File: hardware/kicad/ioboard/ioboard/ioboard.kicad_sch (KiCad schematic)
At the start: 0 parts

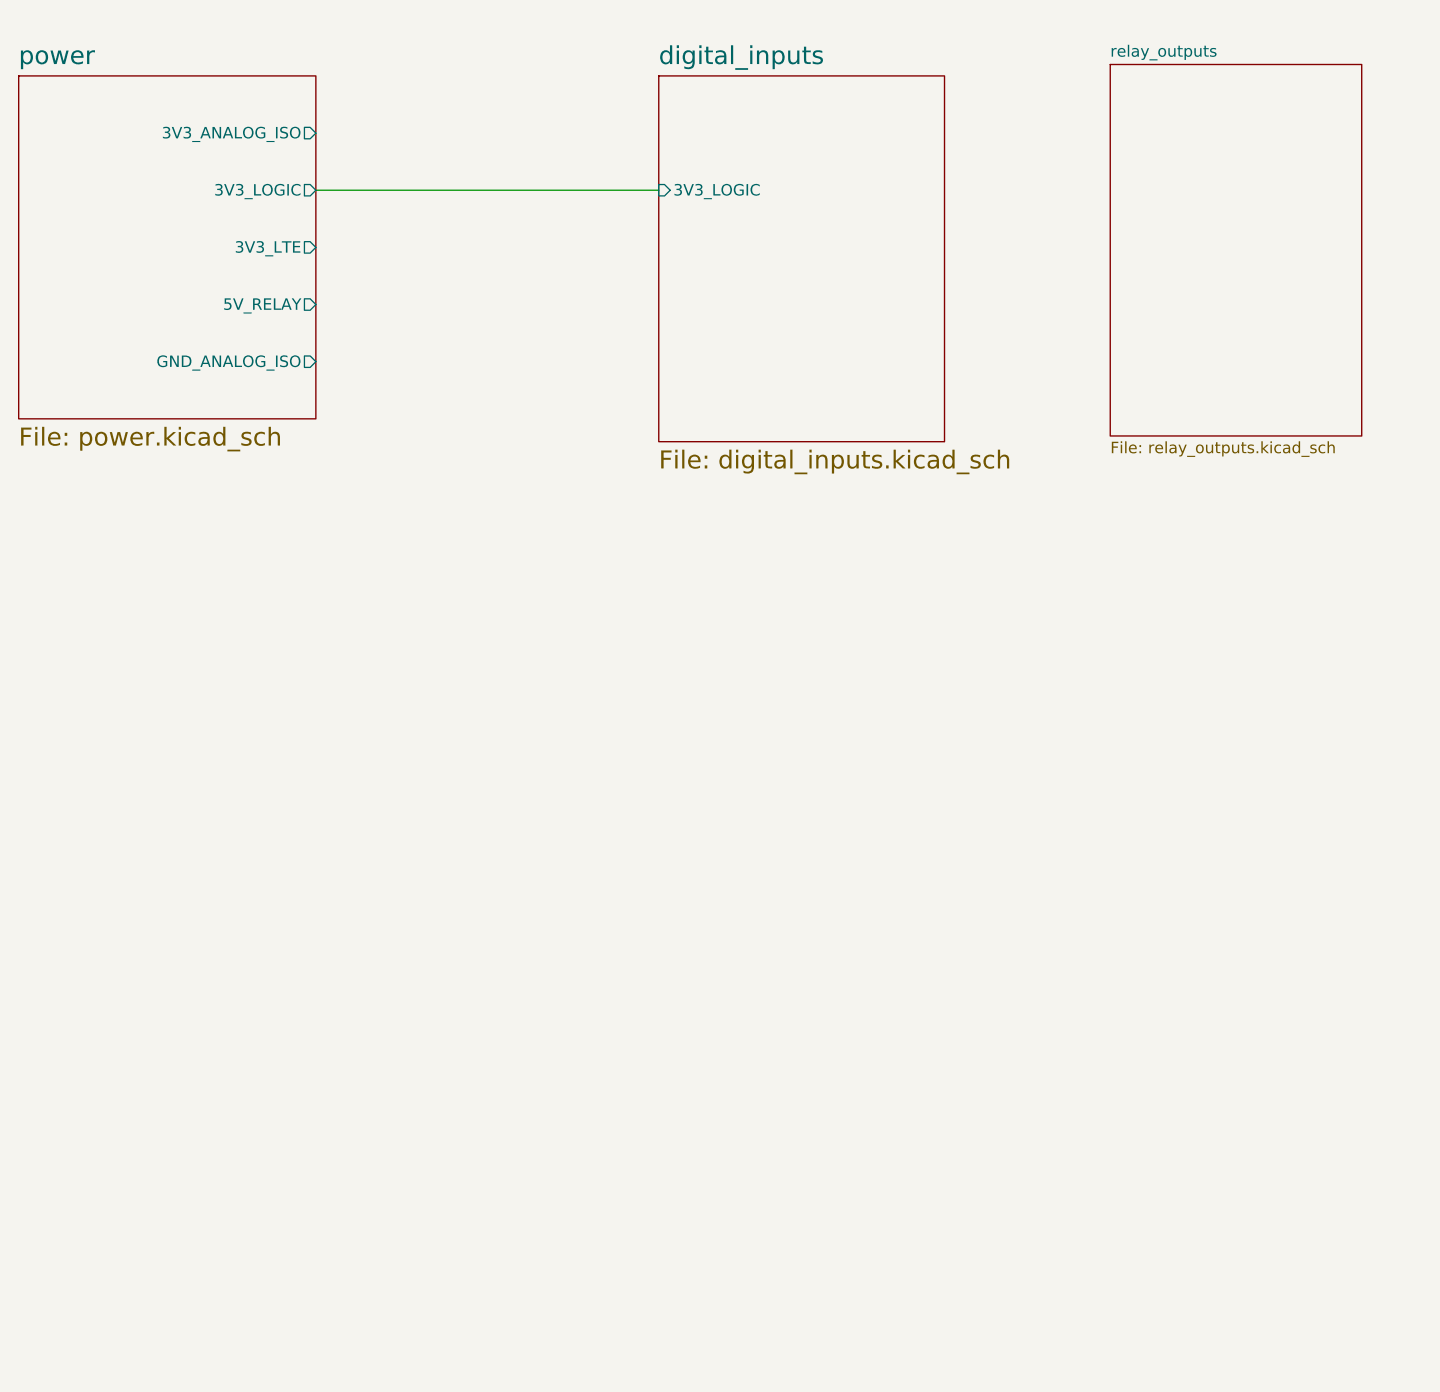
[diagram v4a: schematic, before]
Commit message: relay-outputs: schematic capture complete, plan closed out
All 4 channels wired: K1-K4 (Panasonic ALDP105) driven by Q1-Q4 (Nexperia
MMBT3904) through R26-R33 (510ohm base / 10k pull-down pairs) and D9-D12
(1N4148 flyback), contacts broken out independently to J3 (Phoenix Contact
MC 1,5/8-ST-3,5, 8 positions). Added C21/C22 (10uF/100nF bulk+bypass) at
the 5V_RELAY entry point for EMI/noise reasons -- documented as design
decision 5, with corrected reasoning (coil inductance already rate-limits
the current step, so this isn't about regulator transient response the
way core-compute's WiFi-burst caps were).

Root sheet now wires relay_outputs' 5V_RELAY hierarchical pin to power's
output, verified programmatically that the wire path actually joins both
pin coordinates. Caught and fixed a reversed flyback diode (D9) before
commit -- would have put a forward-biased diode across the coil the whole
time each transistor was on.

Also commits the imported ALDP105 KiCad symbol/footprint library (no
numbered pinout exists in any datasheet, so pin functions were verified
live against the placed symbol, same resolution used for the LTV-247).
The imported footprint has the right pad count but has NOT been
independently checked against the real part's mechanical drawing --
flagged explicitly in the plan doc and CLAUDE.md rather than assumed
correct just because it came from a library.

Documentation: relay-outputs.md completed through sign-off (schematic
capture, verification checklist, acceptance criteria, BOM, commissioning
items), new relay_outputs_bom.csv (23 parts, CSV-parse verified), and
hardware/kicad/README.md updated. ERC and footprint assignment (including
the ALDP105 footprint check) deferred to the same pre-merge pass as
digital-inputs, per the user's standing policy -- tracked in CLAUDE.md.

Co-Authored-By: Claude Sonnet 5 <noreply@anthropic.com>
Claude-Session: https://claude.ai/code/session_011Mk4ACKLUzGL8p2SUjrweQ
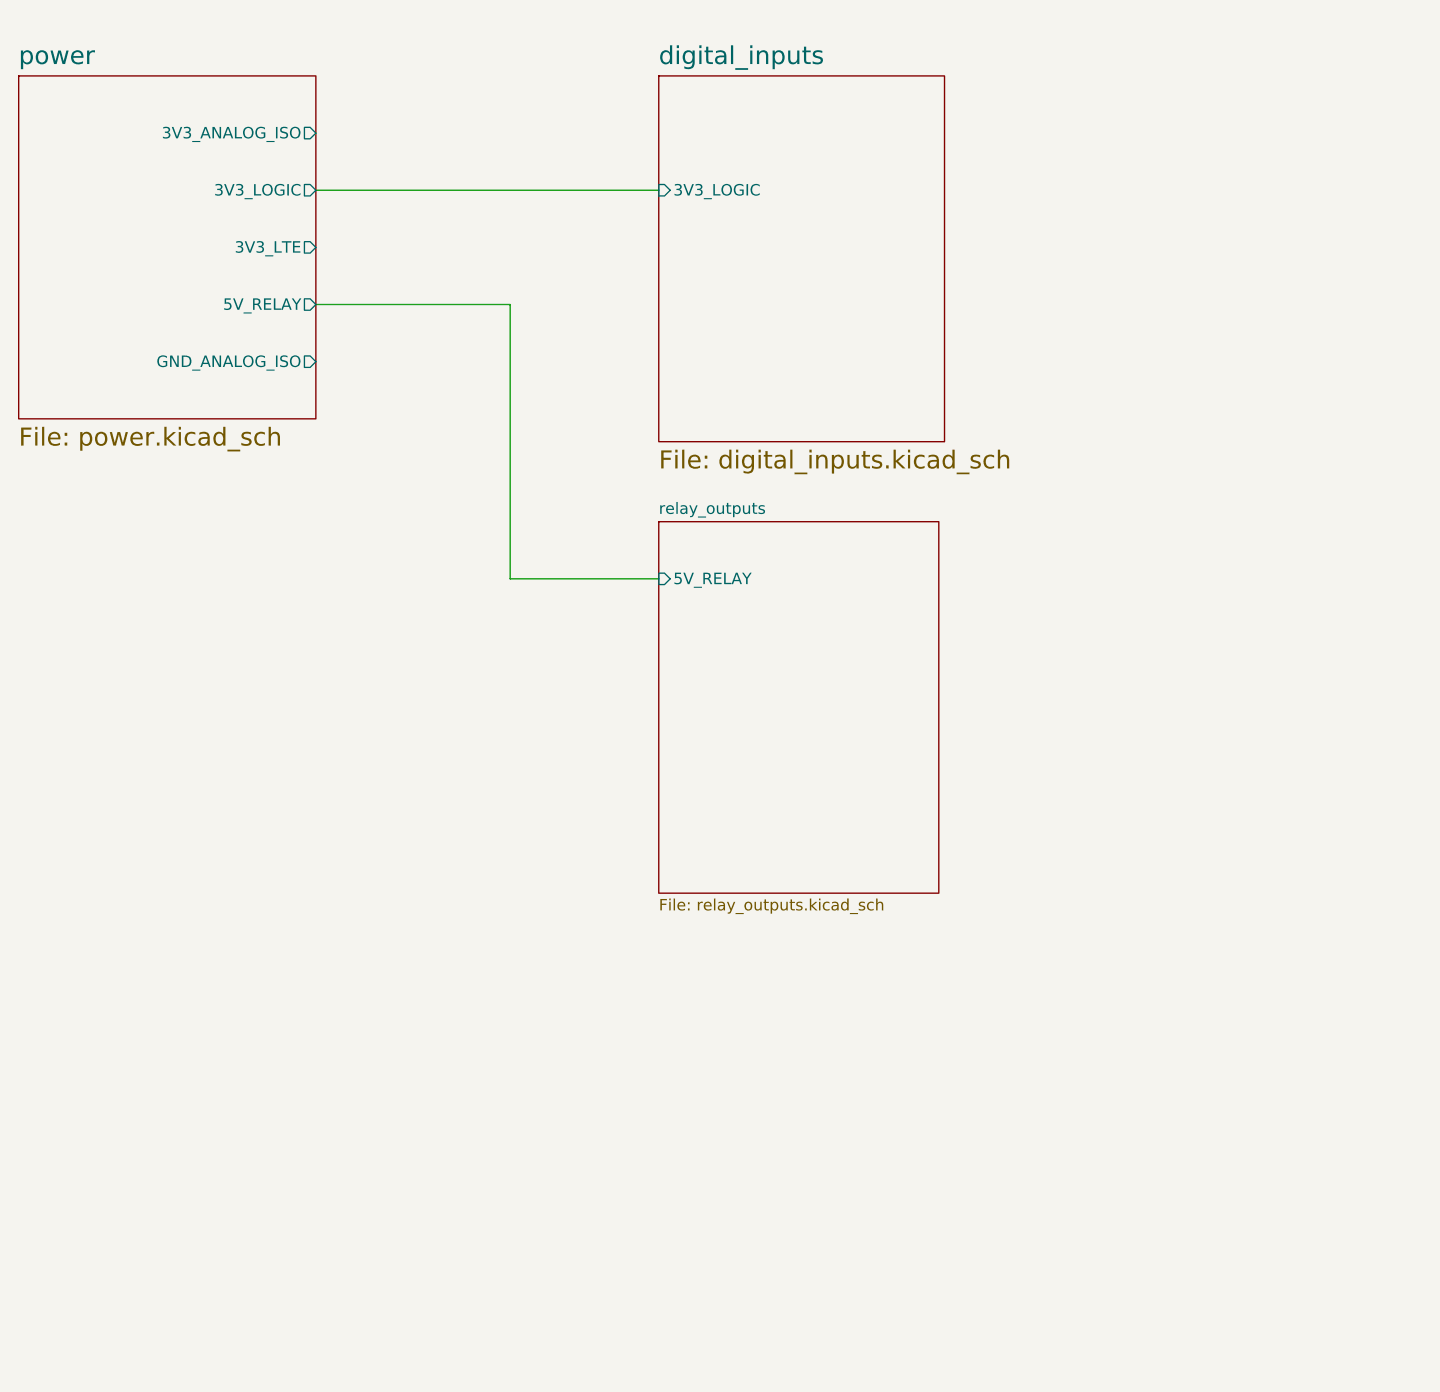
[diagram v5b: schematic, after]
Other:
- sheet relay_outputs ports: added 5V_RELAY; removed none
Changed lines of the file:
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@@
+	(wire
+		(pts
+			(xy 102.87 88.9) (xy 86.36 88.9)
+		)
+		(stroke
+			(width 0)
+			(type default)
+		)
+	)
 	(wire
 		(pts
@@
 		)
 	)
+	(wire
+		(pts
+			(xy 86.36 58.42) (xy 86.36 88.9)
+		)
+		(stroke
+			(width 0)
+			(type default)
+		)
+	)
+	(wire
+		(pts
+			(xy 64.77 58.42) (xy 86.36 58.42)
+		)
+		(stroke
+			(width 0)
+			(type default)
+		)
+	)
 	(sheet
-		(at 153.035 31.75)
-		(size 27.94 41.275)
+		(at 102.87 82.55)
+		(size 31.115 41.275)
 		(exclude_from_sim no)
 		(in_bom yes)
@@
 		)
 		(property "Sheetname" "relay_outputs"
-			(at 153.035 31.0384 0)
+			(at 102.87 81.8384 0)
 			(effects
 				(font
@@
 		)
 		(property "Sheetfile" "relay_outputs.kicad_sch"
-			(at 153.035 73.6096 0)
+			(at 102.87 124.4096 0)
 			(effects
 				(font
@@
 			)
 		)
+		(pin "5V_RELAY" input
+			(at 102.87 88.9 180)
+			(effects
+				(font
+					(size 1.27 1.27)
+				)
+				(justify left)
+			)
+		)

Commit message: analog-io: schematic capture complete, Step 6 verification started
Step 5: analog_io.kicad_sch built and verified pin-by-pin - ADS1115 ADC,
ISO1540 I2C isolator, MCP4725 DAC, 2x LM2904 physical packages (input
buffers + output gain stage), SMBJ15CA TVS protection per channel,
stuffing-option dividers, output feedback network, and the J4 field
connector. Root-sheet integration confirmed on ioboard.kicad_sch.

Two real issues caught and fixed during capture: an output-stage feedback
network wired to break the loop (R_f tied to GND instead of the -/R_in
node), and ambiguous resistor reference designators across the two input
channels.

Step 6: schematic-level verification checks done (address collisions,
ground-domain isolation, feedback topology); ERC and physical bring-up
checks still open.

Co-Authored-By: Claude Sonnet 5 <noreply@anthropic.com>
Claude-Session: https://claude.ai/code/session_011Mk4ACKLUzGL8p2SUjrweQ
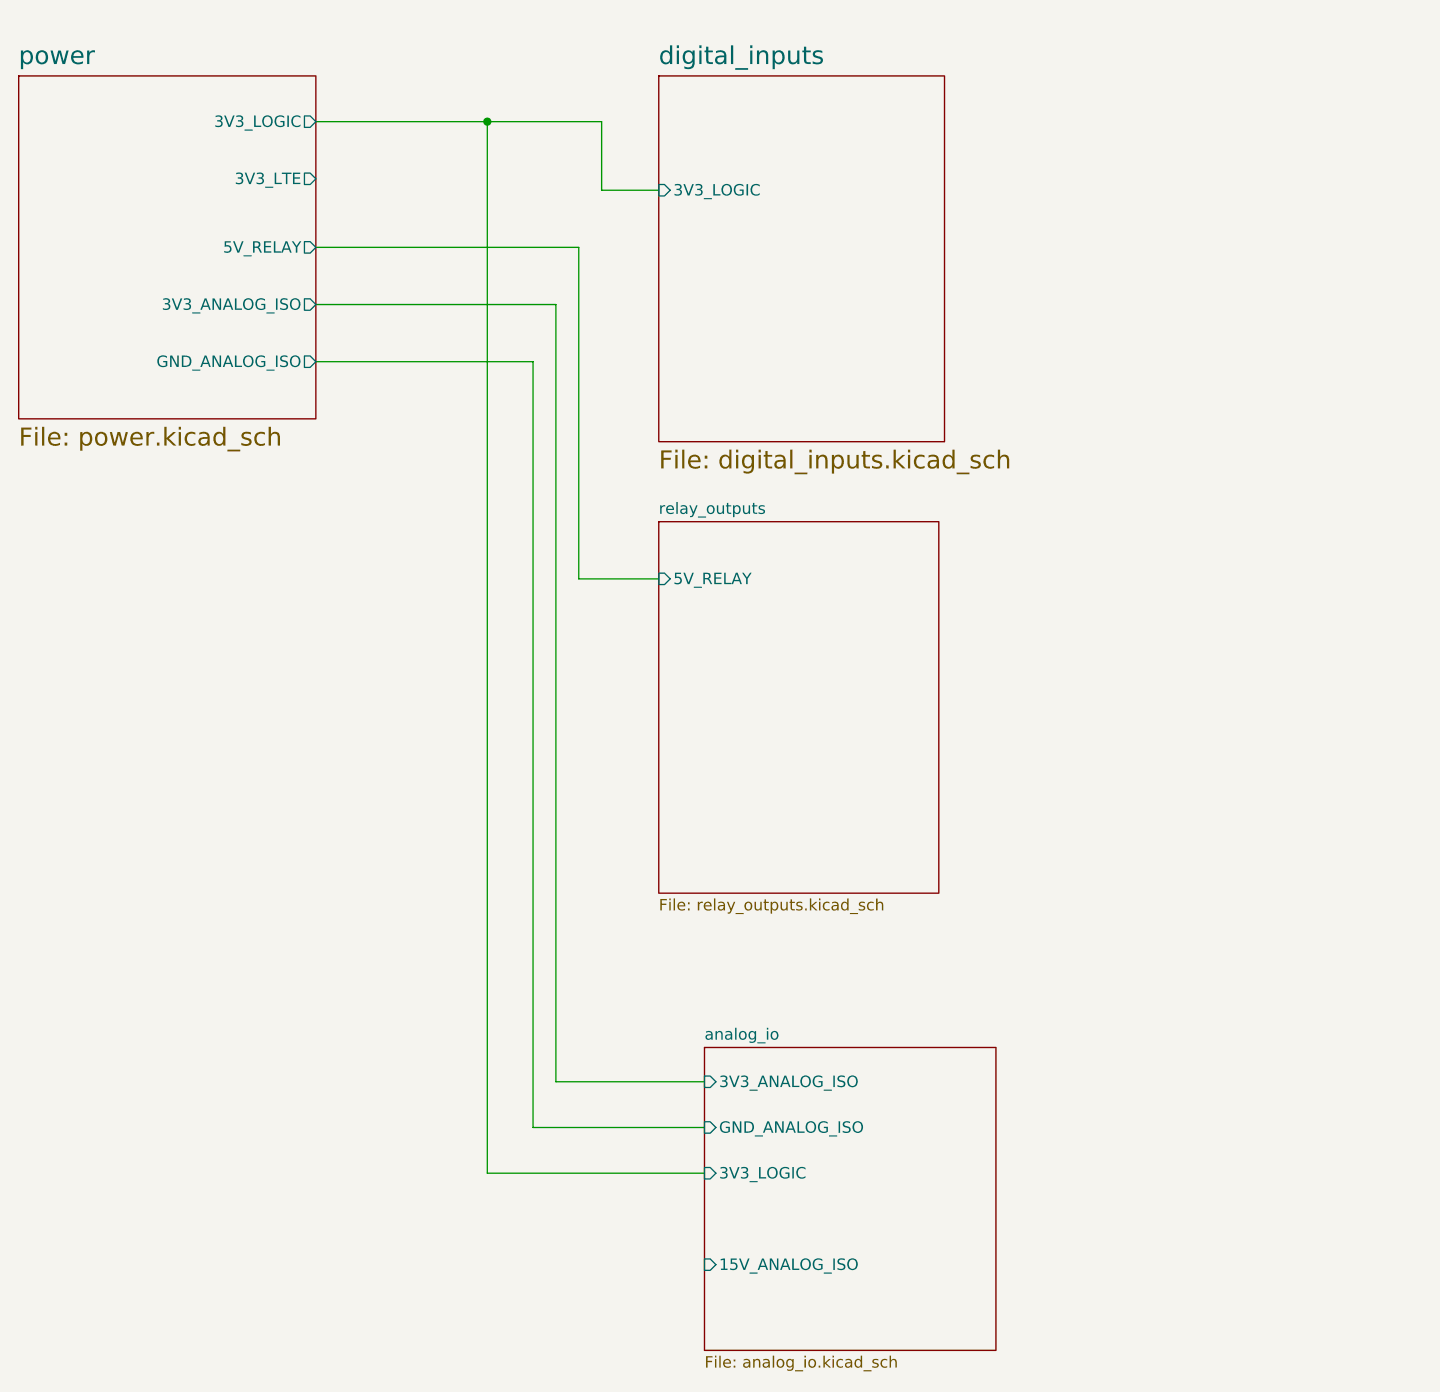
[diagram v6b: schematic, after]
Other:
- added sheet analog_io (analog_io.kicad_sch)
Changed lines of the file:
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@@
 	(generator_version "9.0")
 	(paper "A4")
-	(wire
-		(pts
-			(xy 102.87 88.9) (xy 86.36 88.9)
-		)
-		(stroke
-			(width 0)
-			(type default)
-		)
-	)
-	(wire
-		(pts
-			(xy 64.77 45.72) (xy 102.87 45.72)
-		)
-		(stroke
-			(width 0)
-			(type default)
-		)
-	)
-	(wire
-		(pts
-			(xy 86.36 58.42) (xy 86.36 88.9)
-		)
-		(stroke
-			(width 0)
-			(type default)
-		)
-	)
-	(wire
-		(pts
-			(xy 64.77 58.42) (xy 86.36 58.42)
+	(junction
+		(at 83.82 38.1)
+		(diameter 0)
+		(color 0 0 0 0)
+	)
+	(wire
+		(pts
+			(xy 88.9 64.77) (xy 88.9 149.86)
+		)
+		(stroke
+			(width 0)
+			(type default)
+		)
+	)
+	(wire
+		(pts
+			(xy 102.87 88.9) (xy 93.98 88.9)
+		)
+		(stroke
+			(width 0)
+			(type default)
+		)
+	)
+	(wire
+		(pts
+			(xy 64.77 58.42) (xy 91.44 58.42)
+		)
+		(stroke
+			(width 0)
+			(type default)
+		)
+	)
+	(wire
+		(pts
+			(xy 64.77 52.07) (xy 93.98 52.07)
+		)
+		(stroke
+			(width 0)
+			(type default)
+		)
+	)
+	(wire
+		(pts
+			(xy 96.52 45.72) (xy 102.87 45.72)
+		)
+		(stroke
+			(width 0)
+			(type default)
+		)
+	)
+	(wire
+		(pts
+			(xy 93.98 52.07) (xy 93.98 88.9)
+		)
+		(stroke
+			(width 0)
+			(type default)
+		)
+	)
+	(wire
+		(pts
+			(xy 88.9 149.86) (xy 107.95 149.86)
+		)
+		(stroke
+			(width 0)
+			(type default)
+		)
+	)
+	(wire
+		(pts
+			(xy 64.77 38.1) (xy 83.82 38.1)
+		)
+		(stroke
+			(width 0)
+			(type default)
+		)
+	)
+	(wire
+		(pts
+			(xy 83.82 154.94) (xy 83.82 38.1)
+		)
+		(stroke
+			(width 0)
+			(type default)
+		)
+	)
+	(wire
+		(pts
+			(xy 64.77 64.77) (xy 88.9 64.77)
+		)
+		(stroke
+			(width 0)
+			(type default)
+		)
+	)
+	(wire
+		(pts
+			(xy 91.44 58.42) (xy 91.44 144.78)
+		)
+		(stroke
+			(width 0)
+			(type default)
+		)
+	)
+	(wire
+		(pts
+			(xy 91.44 144.78) (xy 107.95 144.78)
+		)
+		(stroke
+			(width 0)
+			(type default)
+		)
+	)
+	(wire
+		(pts
+			(xy 107.95 154.94) (xy 83.82 154.94)
+		)
+		(stroke
+			(width 0)
+			(type default)
+		)
+	)
+	(wire
+		(pts
+			(xy 96.52 38.1) (xy 96.52 45.72)
+		)
+		(stroke
+			(width 0)
+			(type default)
+		)
+	)
+	(wire
+		(pts
+			(xy 83.82 38.1) (xy 96.52 38.1)
 		)
 		(stroke
@@
 		)
 		(pin "3V3_ANALOG_ISO" output
-			(at 64.77 39.37 0)
+			(at 64.77 58.42 0)
 			(effects
 				(font
@@
 		)
 		(pin "3V3_LOGIC" output
-			(at 64.77 45.72 0)
+			(at 64.77 38.1 0)
 			(effects
 				(font
@@
 		)
 		(pin "3V3_LTE" output
+			(at 64.77 44.45 0)
+			(effects
+				(font
+					(size 1.27 1.27)
+				)
+				(justify right)
+			)
+		)
+		(pin "5V_RELAY" output
 			(at 64.77 52.07 0)
-			(effects
-				(font
-					(size 1.27 1.27)
-				)
-				(justify right)
-			)
-		)
-		(pin "5V_RELAY" output
-			(at 64.77 58.42 0)
 			(effects
 				(font
@@
 				)
 			)
+		)
+	)
+	(sheet
+		(at 107.95 140.97)
+		(size 32.385 33.655)
+		(exclude_from_sim no)
+		(in_bom yes)
+		(on_board yes)
+		(dnp no)
+		(fields_autoplaced yes)
+		(stroke
+			(width 0.1524)
+			(type solid)
+		)
+		(fill
+			(color 0 0 0 0.0000)
+		)
+		(property "Sheetname" "analog_io"
+			(at 107.95 140.2584 0)
+			(effects
+				(font
+					(size 1.27 1.27)
+				)
+				(justify left bottom)
+			)
+		)
+		(property "Sheetfile" "analog_io.kicad_sch"
+			(at 107.95 175.2096 0)
+			(effects
+				(font
+					(size 1.27 1.27)
+				)
+				(justify left top)
+			)
+		)
+		(pin "3V3_ANALOG_ISO" input
+			(at 107.95 144.78 180)
+			(effects
+				(font
+					(size 1.27 1.27)
+				)
+				(justify left)
+			)
+		)
+		(pin "15V_ANALOG_ISO" input
+			(at 107.95 165.1 180)
+			(effects
+				(font
+					(size 1.27 1.27)
+				)
+				(justify left)
+			)
+		)
+		(pin "GND_ANALOG_ISO" input
+			(at 107.95 149.86 180)
+			(effects
+				(font
+					(size 1.27 1.27)
+				)
+				(justify left)
+			)
+		)
+		(pin "3V3_LOGIC" input
+			(at 107.95 154.94 180)
+			(effects
+				(font
+					(size 1.27 1.27)
+				)
+				(justify left)
+			)
+		)
+		(instances
+			(project "ioboard"
+				(path "/a0fa9f92-ef51-408b-9617-1545f9e9dad8"
+					(page "5")
+				)
+			)
